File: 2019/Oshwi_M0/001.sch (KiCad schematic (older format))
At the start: 71 parts, among them CN1 MICROSD, IC1 APX803, J1 Conn_01x01, J10 Conn_01x01, J11 Conn_01x01, J12 Conn_01x01, J2 Conn_01x01, J3 Conn_01x01, J4 Conn_01x01, J5 Conn_01x01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

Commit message: Add Schematic for TFT & PyPortal
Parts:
- CHG1, L1: symbol Device:LED -> 001-rescue:LED-Device
- J1, J10, J11, J12, J2, J3, J4, J5, J6, J7, J8, J9, J? (x16): symbol Connector:Conn_01x01_Female -> 001-rescue:Conn_01x01_Female-Connector
- SW1: symbol Switch:SW_Push -> 001-rescue:SW_Push-Switch
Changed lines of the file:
@@
 Connection ~ 1000 4200
 $Comp
-L Device:LED CHG1
+L 001-rescue:LED-Device CHG1
 U 1 1 5CCC697A
 P 6150 1525
@@
 $EndComp
 $Comp
-L Device:LED L1
+L 001-rescue:LED-Device L1
 U 1 1 5CCCC16E
 P 10250 5125
@@
 $EndComp
 $Comp
-L Switch:SW_Push SW1
+L 001-rescue:SW_Push-Switch SW1
 U 1 1 5CC54900
 P 5450 1375
@@
 $EndComp
 $Comp
-L Connector:Conn_01x01_Female J1
+L 001-rescue:Conn_01x01_Female-Connector J1
 U 1 1 5CC4E09B
 P 7350 4175
@@
 $EndComp
 $Comp
-L Connector:Conn_01x01_Female J2
+L 001-rescue:Conn_01x01_Female-Connector J2
 U 1 1 5CC50EE1
 P 7350 4275
@@
 $EndComp
 $Comp
-L Connector:Conn_01x01_Female J3
+L 001-rescue:Conn_01x01_Female-Connector J3
 U 1 1 5CC51194
 P 7350 4375
@@
 $EndComp
 $Comp
-L Connector:Conn_01x01_Female J4
+L 001-rescue:Conn_01x01_Female-Connector J4
 U 1 1 5CC5239F
 P 7350 4475
@@
 $EndComp
 $Comp
-L Connector:Conn_01x01_Female J5
+L 001-rescue:Conn_01x01_Female-Connector J5
 U 1 1 5CC523AA
 P 7350 4575
@@
 $EndComp
 $Comp
-L Connector:Conn_01x01_Female J6
+L 001-rescue:Conn_01x01_Female-Connector J6
 U 1 1 5CC523B5
 P 7350 4675
@@
 $EndComp
 $Comp
-L Connector:Conn_01x01_Female J7
+L 001-rescue:Conn_01x01_Female-Connector J7
 U 1 1 5CC54BD1
 P 7350 4775
@@
 $EndComp
 $Comp
-L Connector:Conn_01x01_Female J8
+L 001-rescue:Conn_01x01_Female-Connector J8
 U 1 1 5CC54BDC
 P 7350 4875
@@
 $EndComp
 $Comp
-L Connector:Conn_01x01_Female J9
+L 001-rescue:Conn_01x01_Female-Connector J9
 U 1 1 5CC54BE7
 P 7350 4975
@@
 $EndComp
 $Comp
-L Connector:Conn_01x01_Female J10
+L 001-rescue:Conn_01x01_Female-Connector J10
 U 1 1 5CC54BF2
 P 7350 5075
@@
 $EndComp
 $Comp
-L Connector:Conn_01x01_Female J11
+L 001-rescue:Conn_01x01_Female-Connector J11
 U 1 1 5CC54BFD
 P 7350 5175
@@
 $EndComp
 $Comp
-L Connector:Conn_01x01_Female J12
+L 001-rescue:Conn_01x01_Female-Connector J12
 U 1 1 5CC54C08
 P 7350 5275
@@
 $EndComp
 $Comp
-L Connector:Conn_01x01_Female J?
+L 001-rescue:Conn_01x01_Female-Connector J?
 U 1 1 5CC5B3C7
 P 9150 4175
@@
 $EndComp
 $Comp
-L Connector:Conn_01x01_Female J?
+L 001-rescue:Conn_01x01_Female-Connector J?
 U 1 1 5CC5B3D2
 P 9150 4275
@@
 $EndComp
 $Comp
-L Connector:Conn_01x01_Female J?
+L 001-rescue:Conn_01x01_Female-Connector J?
 U 1 1 5CC5B3DD
 P 9150 4400
@@
 $EndComp
 $Comp
-L Connector:Conn_01x01_Female J?
+L 001-rescue:Conn_01x01_Female-Connector J?
 U 1 1 5CC5B3F3
 P 9150 4600
@@
 $EndComp
 $Comp
-L Connector:Conn_01x01_Female J?
+L 001-rescue:Conn_01x01_Female-Connector J?
 U 1 1 5CC5B3FE
 P 9150 4700
@@
 $EndComp
 $Comp
-L Connector:Conn_01x01_Female J?
+L 001-rescue:Conn_01x01_Female-Connector J?
 U 1 1 5CC5B409
 P 9150 4800
@@
 $EndComp
 $Comp
-L Connector:Conn_01x01_Female J?
+L 001-rescue:Conn_01x01_Female-Connector J?
 U 1 1 5CC5B414
 P 9150 4900
@@
 $EndComp
 $Comp
-L Connector:Conn_01x01_Female J?
+L 001-rescue:Conn_01x01_Female-Connector J?
 U 1 1 5CC5B41F
 P 9150 5000
@@
 $EndComp
 $Comp
-L Connector:Conn_01x01_Female J?
+L 001-rescue:Conn_01x01_Female-Connector J?
 U 1 1 5CC5B42A
 P 9150 5100
@@
 $EndComp
 $Comp
-L Connector:Conn_01x01_Female J?
+L 001-rescue:Conn_01x01_Female-Connector J?
 U 1 1 5CC5B435
 P 9150 5200
@@
 $EndComp
 $Comp
-L Connector:Conn_01x01_Female J?
+L 001-rescue:Conn_01x01_Female-Connector J?
 U 1 1 5CC5B440
 P 9150 5300
@@
 $EndComp
 $Comp
-L Connector:Conn_01x01_Female J?
+L 001-rescue:Conn_01x01_Female-Connector J?
 U 1 1 5CC62A14
 P 9150 5400
@@
 $EndComp
 $Comp
-L Connector:Conn_01x01_Female J?
+L 001-rescue:Conn_01x01_Female-Connector J?
 U 1 1 5CC62A1F
 P 9150 5500
@@
 $EndComp
 $Comp
-L Connector:Conn_01x01_Female J?
+L 001-rescue:Conn_01x01_Female-Connector J?
 U 1 1 5CC62A2A
 P 9150 5600
@@
 $EndComp
 $Comp
-L Connector:Conn_01x01_Female J?
+L 001-rescue:Conn_01x01_Female-Connector J?
 U 1 1 5CC64120
 P 9150 5700
@@
 	8350 4400 8950 4400
 $Comp
-L Connector:Conn_01x01_Female J?
+L 001-rescue:Conn_01x01_Female-Connector J?
 U 1 1 5CC71CF1
 P 9150 4500

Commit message: Minors updates
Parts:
- removed JP2: HEADER-1X16ROUND, Oshwi_M0:1X16_ROUND, symbol 001-rescue:HEADER-1X16ROUND-Adafruit_Feather_M0_Express-eagle-import
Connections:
- wire segments 219 -> 217
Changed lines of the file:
@@
 	10250 5275 10250 5375
-Wire Wire Line
-	9800 6475 10200 6475
-Wire Wire Line
-	10400 6600 10400 6700
 Wire Wire Line
 	3450 2275 3450 1975
@@
 $EndComp
 $Comp
-L 001-rescue:HEADER-1X16ROUND-Adafruit_Feather_M0_Express-eagle-import JP2
-U 1 1 5CCCC11E
-P 9125 7275
-F 0 "JP2" H 8875 8100 59  0000 L BNN
-F 1 "HEADER-1X16ROUND" H 8875 6275 59  0000 L BNN
-F 2 "Oshwi_M0:1X16_ROUND" H 9125 7275 50  0001 C CNN
-F 3 "" H 9125 7275 50  0001 C CNN
-	1    9125 7275
-	-1   0    0    1
-$EndComp
-$Comp

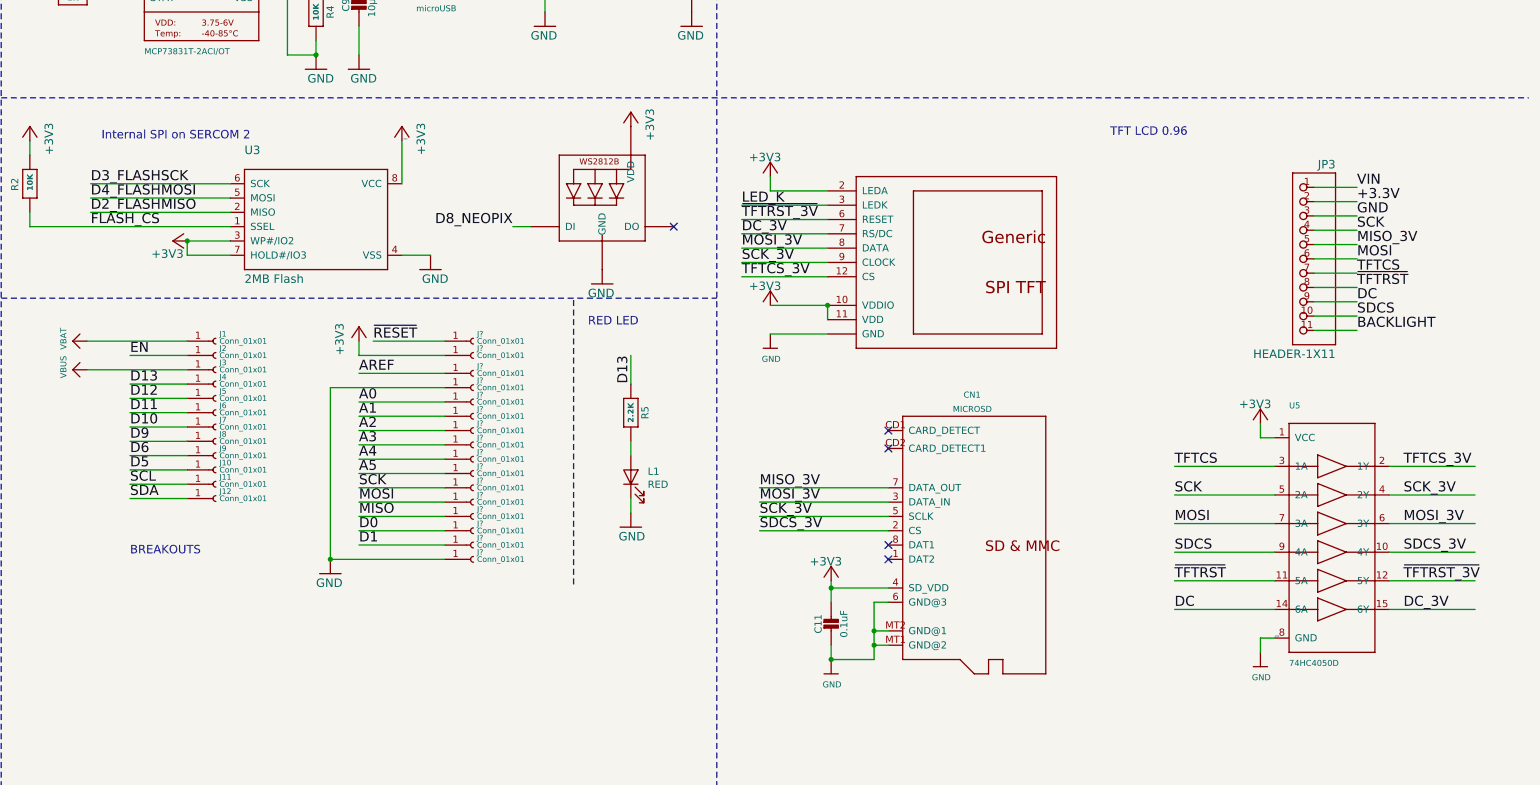
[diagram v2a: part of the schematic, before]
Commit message: More examples TFTs
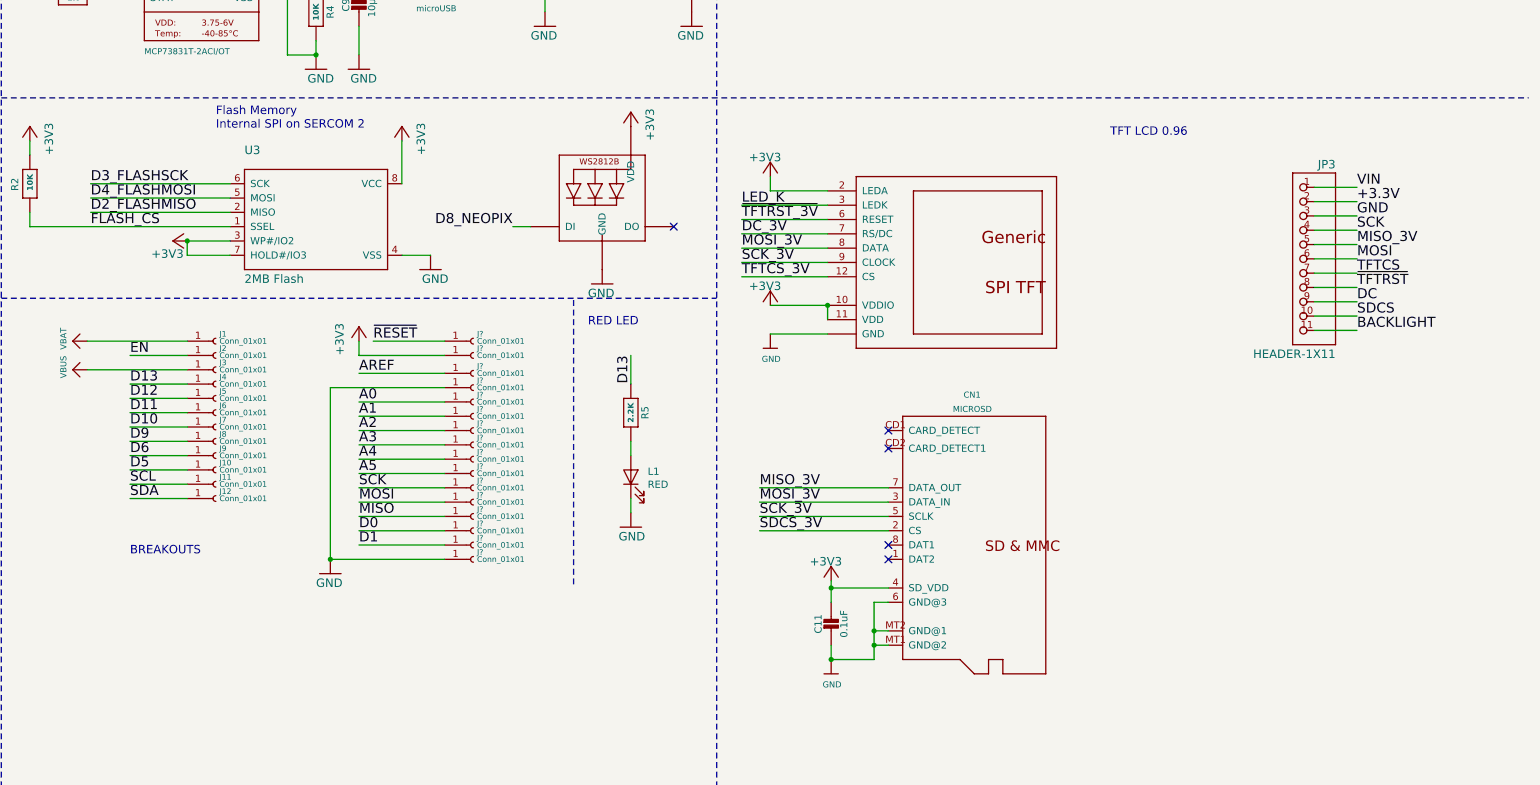
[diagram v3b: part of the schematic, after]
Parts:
- removed U5: 74HC4050D, Adafruit 0.96in 160x80 TFT Display:SOIC16, symbol Adafruit_0.96in_160x80_TFT_Display-eagle-import:74HC4050D
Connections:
- net +3V3: no longer names the net of U3.8 (VCC)
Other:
- note added: "Flash Memory \nInternal SPI on SERCOM 2"
- note removed: "Internal SPI on SERCOM 2"
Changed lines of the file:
@@
 Wire Wire Line
 	8650 2775 8650 3075
-Text Label 8650 2775 0    10   ~ 0
-+3V3
 Wire Wire Line
 	7450 3475 7150 3475
@@
 Text Notes 9950 4075 0    59   ~ 0
 RED LED
-Text Notes 6550 2775 0    59   ~ 0
-Internal SPI on SERCOM 2
 Wire Notes Line
 	750  2575 5850 2575
@@
 $EndComp
 $Comp
-L Adafruit_0.96in_160x80_TFT_Display-eagle-import:74HC4050D U5
-U 1 1 E770509E
-P 15150 5550
-F 0 "U5" H 14850 6450 42  0000 L BNN
-F 1 "74HC4050D" H 14850 4650 42  0000 L BNN
-F 2 "Adafruit 0.96in 160x80 TFT Display:SOIC16" H 15150 5550 50  0001 C CNN
-F 3 "" H 15150 5550 50  0001 C CNN
-	1    15150 5550
-	1    0    0    -1
-$EndComp
-$Comp
-L Adafruit_0.96in_160x80_TFT_Display-eagle-import:GND #U$036
-U 1 1 5CCCC11B
-P 14650 6450
-F 0 "#U$036" H 14650 6450 50  0001 C CNN
-F 1 "GND" H 14590 6350 42  0000 L BNN
-F 2 "" H 14650 6450 50  0001 C CNN
-F 3 "" H 14650 6450 50  0001 C CNN
-	1    14650 6450
-	1    0    0    -1
-$EndComp
-$Comp
 L Adafruit_0.96in_160x80_TFT_Display-eagle-import:GND #U$028
 U 1 1 D872CB34
@@
 	-1   0    0    -1
 $EndComp
-Text Label 14050 5050 0    70   ~ 0
-TFTCS
-Wire Wire Line
-	14750 5050 14050 5050
 Text Label 15325 3700 0    70   ~ 0
 TFTCS
@@
 Wire Wire Line
 	15000 8125 14500 8125
-Text Label 14050 5850 0    70   ~ 0
-~TFTRST
-Wire Wire Line
-	14750 5850 14050 5850
 Text Label 15325 3800 0    70   ~ 0
 ~TFTRST
-Text Label 15650 5650 0    70   ~ 0
-SDCS_3V
-Wire Wire Line
-	15550 5650 16150 5650
 Text Label 11150 5500 0    70   ~ 0
 SDCS_3V
 Wire Wire Line
 	12050 5500 11150 5500
-Text Label 15650 5450 0    70   ~ 0
-MOSI_3V
-Wire Wire Line
-	15550 5450 16150 5450
 Text Label 11025 3525 0    70   ~ 0
 MOSI_3V
@@
 Wire Wire Line
 	11625 3225 11025 3225
-Text Label 14050 5650 0    70   ~ 0
-SDCS
-Wire Wire Line
-	14750 5650 14050 5650
 Text Label 15325 4000 0    70   ~ 0
 SDCS
 Text Label 15325 3100 0    70   ~ 0
 VIN
-Text Label 15650 6050 0    70   ~ 0
-DC_3V
-Wire Wire Line
-	15550 6050 16150 6050
 Text Label 11025 3425 0    70   ~ 0
 DC_3V
 Wire Wire Line
 	11625 3425 11025 3425
-Text Label 15650 5850 0    70   ~ 0
-~TFTRST_3V
-Wire Wire Line
-	15550 5850 16150 5850
 Text Label 11025 3325 0    70   ~ 0
 ~TFTRST_3V
 Wire Wire Line
 	11625 3325 11025 3325
-Text Label 15650 5250 0    70   ~ 0
-SCK_3V
-Wire Wire Line
-	15550 5250 16150 5250
 Text Label 11025 3625 0    70   ~ 0
 SCK_3V
@@
 Wire Wire Line
 	12050 5400 11150 5400
-Text Label 14050 6050 0    70   ~ 0
-DC
-Wire Wire Line
-	14750 6050 14050 6050
 Text Label 15325 3900 0    70   ~ 0
 DC
-Text Label 14050 5450 0    70   ~ 0
-MOSI
-Wire Wire Line
-	14750 5450 14050 5450
 Text Label 15325 3600 0    70   ~ 0
 MOSI
-Text Label 14050 5250 0    70   ~ 0
-SCK
-Wire Wire Line
-	14750 5250 14050 5250
 Text Label 15325 3400 0    70   ~ 0
 SCK
-Text Label 15650 5050 0    70   ~ 0
-TFTCS_3V
-Wire Wire Line
-	16150 5050 15550 5050
 Text Label 11025 3725 0    70   ~ 0
 TFTCS_3V
@@
 +3.3V
 Wire Wire Line
-	14650 4850 14750 4850
-Wire Wire Line
-	14650 4750 14650 4850
-Wire Wire Line
 	11650 5900 11650 6000
 Wire Wire Line
@@
 Wire Wire Line
 	13025 8350 13025 8550
-Text Label 14750 6250 0    10   ~ 0
-GND
-Wire Wire Line
-	14650 6250 14650 6350
-Wire Wire Line
-	14750 6250 14650 6250
 Connection ~ 11950 6200
 Connection ~ 11950 6300
@@
 $EndComp
 $Comp
-L 001-rescue:+3V3-Adafruit_Feather_M0_Express-eagle-import #+3V0103
-U 1 1 5CC63AC6
-P 14650 4650
-F 0 "#+3V0103" H 14650 4650 50  0001 C CNN
-F 1 "+3V3" H 14500 4650 59  0000 L BNN
-F 2 "" H 14650 4650 50  0001 C CNN
-F 3 "" H 14650 4650 50  0001 C CNN
-	1    14650 4650
-	1    0    0    -1
-$EndComp
-$Comp
 L 001-rescue:+3V3-Adafruit_Feather_M0_Express-eagle-import #+3V0104
 U 1 1 5CC64777
@@
 	8150 5700 8950 5700
 Connection ~ 8150 5700
+Text Notes 7350 2700 0    59   ~ 0
+Flash Memory \nInternal SPI on SERCOM 2
 $EndSCHEMATC
